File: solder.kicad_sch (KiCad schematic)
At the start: 8 parts, among them M1 Motor_DC, SW1 SW_Push, SW2 SW_Push

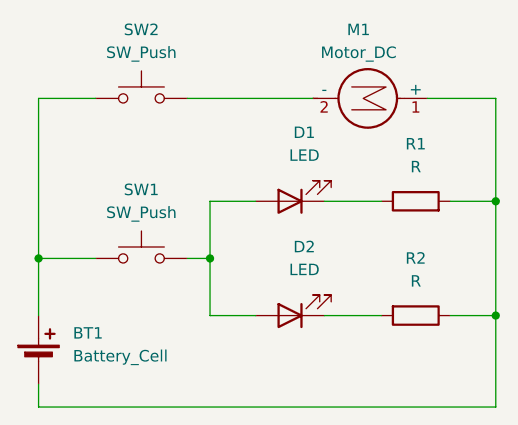
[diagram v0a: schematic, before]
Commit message: rotated motor
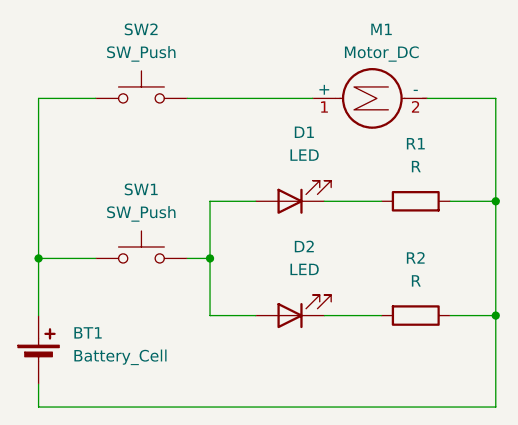
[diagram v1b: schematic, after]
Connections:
- net at BT1.2 (-), R1.2, R2.1: now also M1.2 (-); no longer M1.1 (+)
- net at SW2.2: now also M1.1 (+); no longer M1.2 (-)
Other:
- moved on the sheet: M1
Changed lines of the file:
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@@
+	(wire
+		(pts
+			(xy 105.41 53.34) (xy 105.41 59.69)
+		)
+		(stroke
+			(width 0)
+			(type default)
+		)
+	)
+	(wire
+		(pts
+			(xy 118.11 46.99) (xy 124.46 46.99)
+		)
+		(stroke
+			(width 0)
+			(type default)
+		)
+	)
+	(wire
+		(pts
+			(xy 132.08 46.99) (xy 137.16 46.99)
+		)
+		(stroke
+			(width 0)
+			(type default)
+		)
+	)
+	(wire
+		(pts
+			(xy 86.36 59.69) (xy 86.36 53.34)
+		)
+		(stroke
+			(width 0)
+			(type default)
+		)
+	)
 	(wire
 		(pts
 			(xy 129.54 35.56) (xy 137.16 35.56)
-		)
-		(stroke
-			(width 0)
-			(type default)
-		)
-	)
-	(wire
-		(pts
-			(xy 105.41 53.34) (xy 105.41 59.69)
-		)
-		(stroke
-			(width 0)
-			(type default)
-		)
-	)
-	(wire
-		(pts
-			(xy 118.11 46.99) (xy 124.46 46.99)
-		)
-		(stroke
-			(width 0)
-			(type default)
-		)
-	)
-	(wire
-		(pts
-			(xy 132.08 46.99) (xy 137.16 46.99)
-		)
-		(stroke
-			(width 0)
-			(type default)
-		)
-	)
-	(wire
-		(pts
-			(xy 86.36 59.69) (xy 86.36 53.34)
 		)
 		(stroke
@@
 	(symbol
 		(lib_id "Motor:Motor_DC")
-		(at 124.46 35.56 270)
+		(at 121.92 35.56 90)
 		(unit 1)
 		(exclude_from_sim no)
@@
 		(fields_autoplaced yes)
 		(property "Reference" "M1"
-			(at 121.92 27.94 90)
+			(at 124.46 27.94 90)
 			(effects
 				(font
@@
 		)
 		(property "Value" "Motor_DC"
-			(at 121.92 30.48 90)
+			(at 124.46 30.48 90)
 			(effects
 				(font
@@
 		)
 		(property "Footprint" "Connector_PinHeader_2.54mm:PinHeader_1x02_P2.54mm_Vertical"
-			(at 122.174 35.56 0)
+			(at 124.206 35.56 0)
 			(effects
 				(font
@@
 		)
 		(property "Datasheet" "~"
-			(at 122.174 35.56 0)
+			(at 124.206 35.56 0)
 			(effects
 				(font
@@
 		)
 		(property "Description" "DC Motor"
-			(at 124.46 35.56 0)
-			(effects
-				(font
+			(at 121.92 35.56 0)
+			(effects
+				(font
